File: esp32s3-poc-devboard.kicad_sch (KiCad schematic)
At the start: 23 parts, among them J1 24VDC, J2 Conn_01x01_Pin, U1 ESP32-S3, U2 AMS1117-3.3, U3 XC6206P332MR, U4 TPS5430DDA

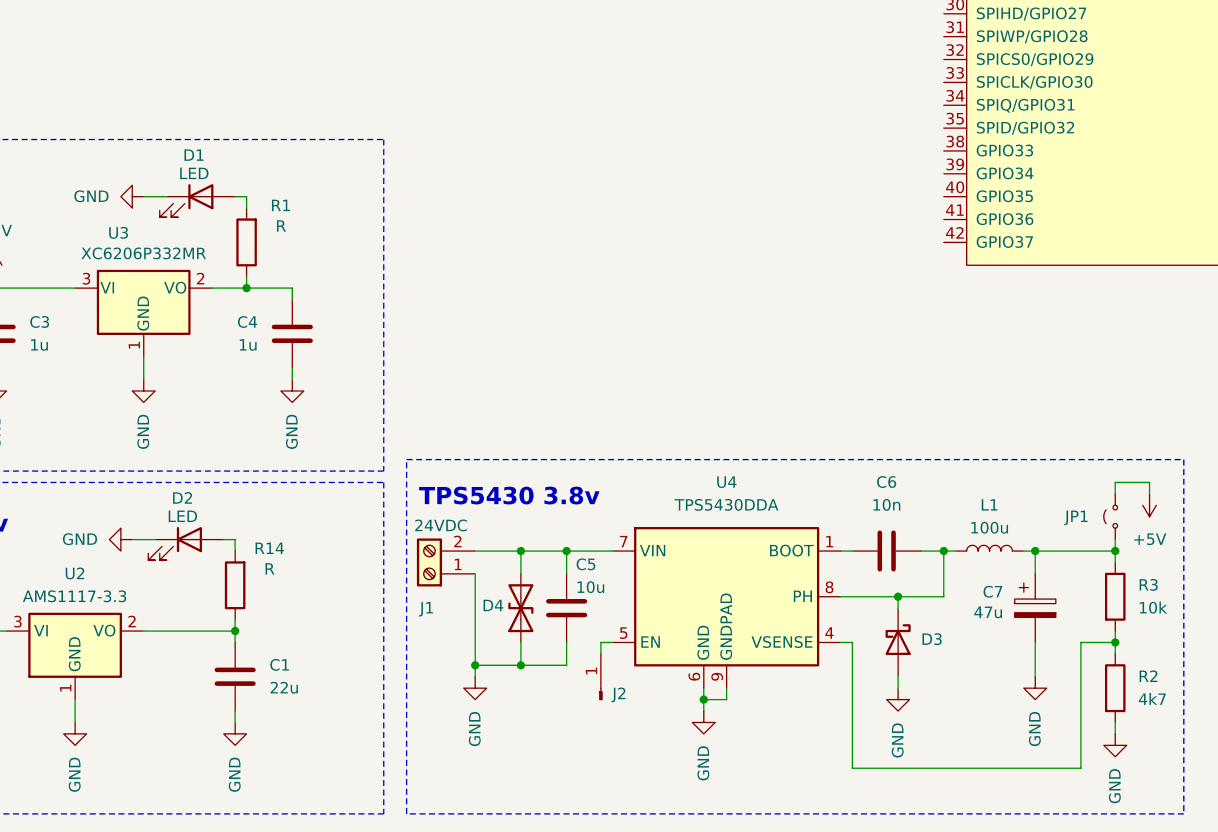
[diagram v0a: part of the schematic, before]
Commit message: add 3v3 power selection jumper
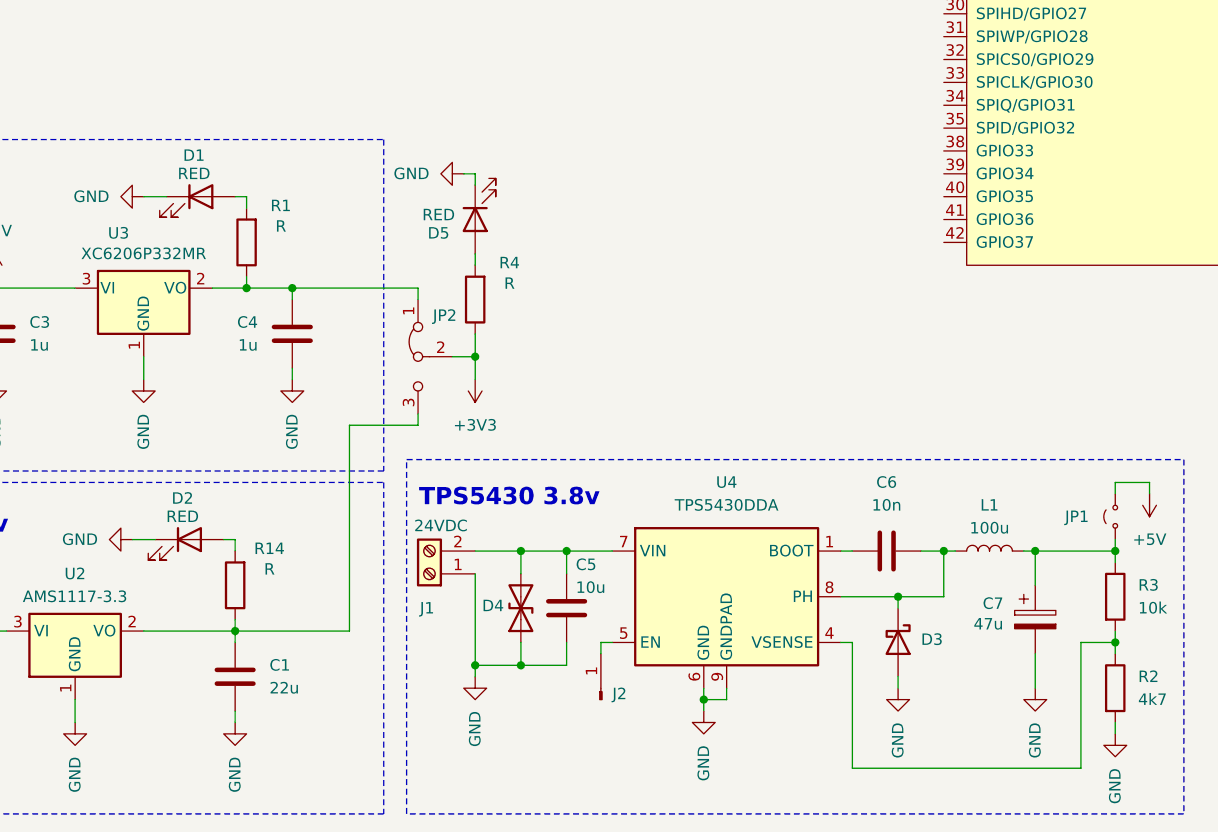
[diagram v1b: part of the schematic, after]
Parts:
- added D5: RED, symbol Device:LED
- added JP2: Jumper_3_Bridged12, symbol Jumper:Jumper_3_Bridged12
- added R4: R, symbol Device:R
- D1, D2: value LED -> RED
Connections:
- net GND: now also D5.1 (K)
- net at C4.1, R1.1, U3.2 (VO): now also JP2.1 (A)
- net at C1.1, R14.1, U2.2 (VO): now also JP2.3 (B)
- new net: D5.2 (A), R4.2
- new net +3V3: JP2.2 (C), R4.1
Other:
- moved on the sheet: C7

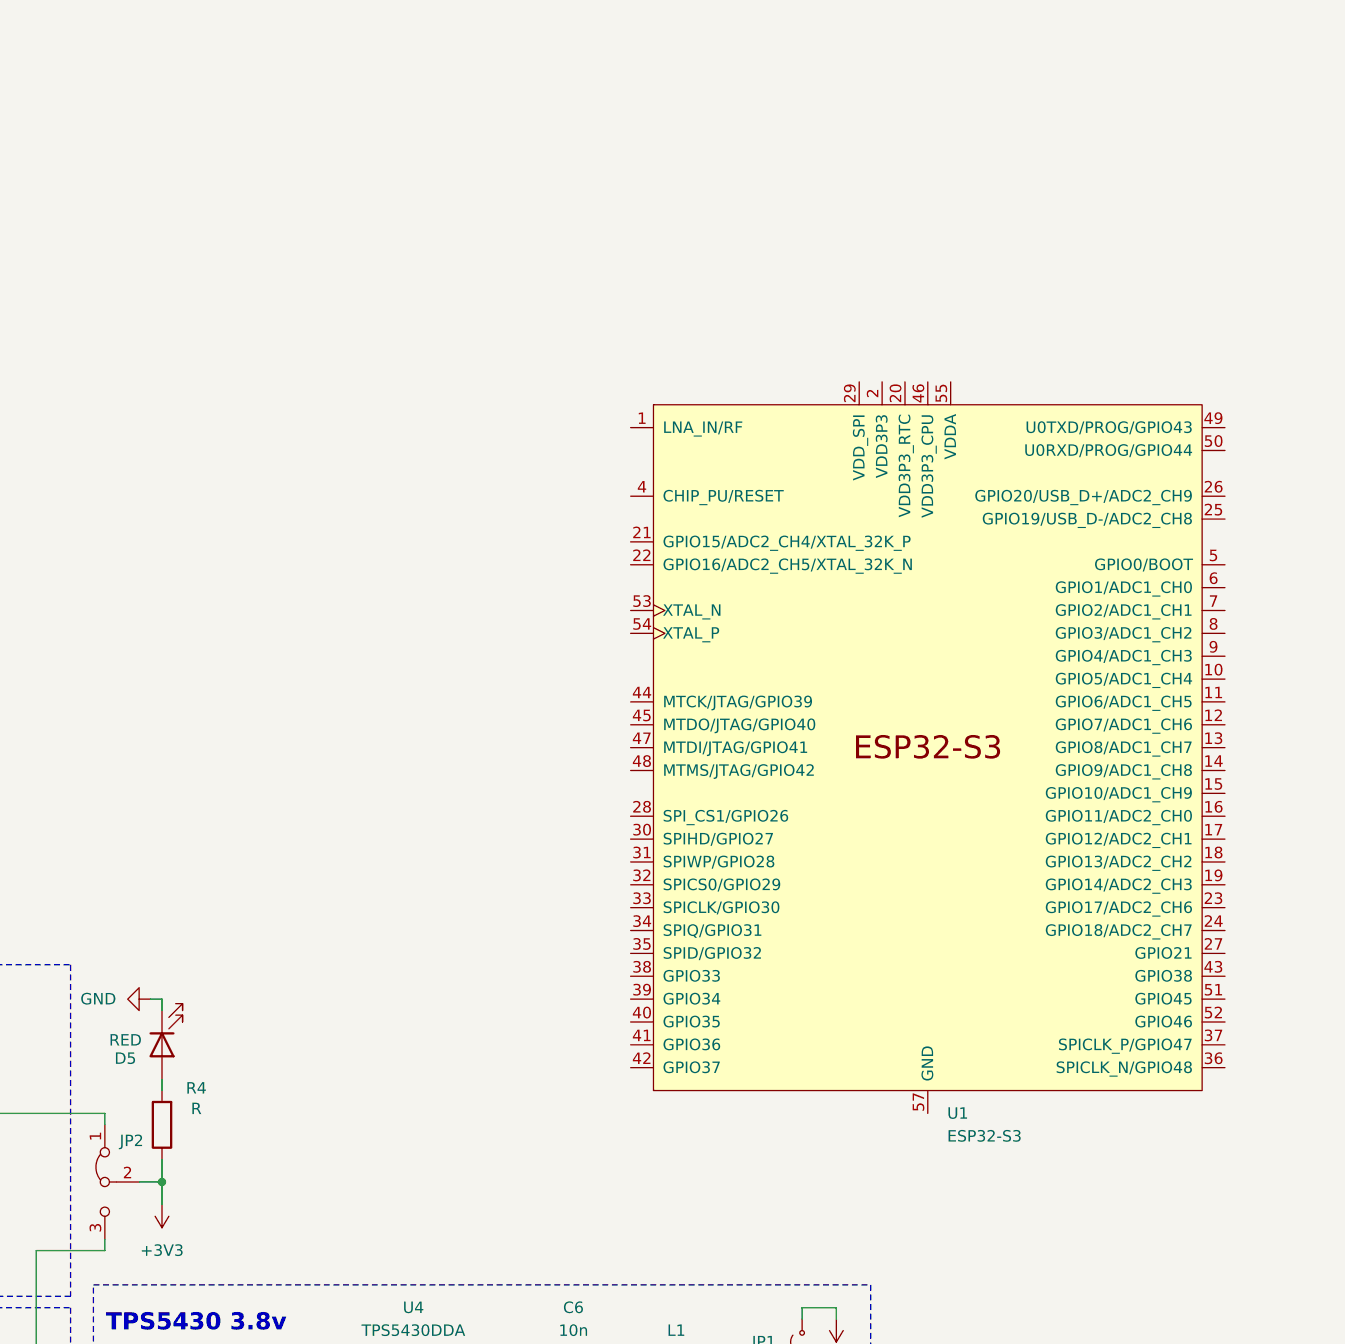
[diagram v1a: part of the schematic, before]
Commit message: add mcu power strapping capacitors
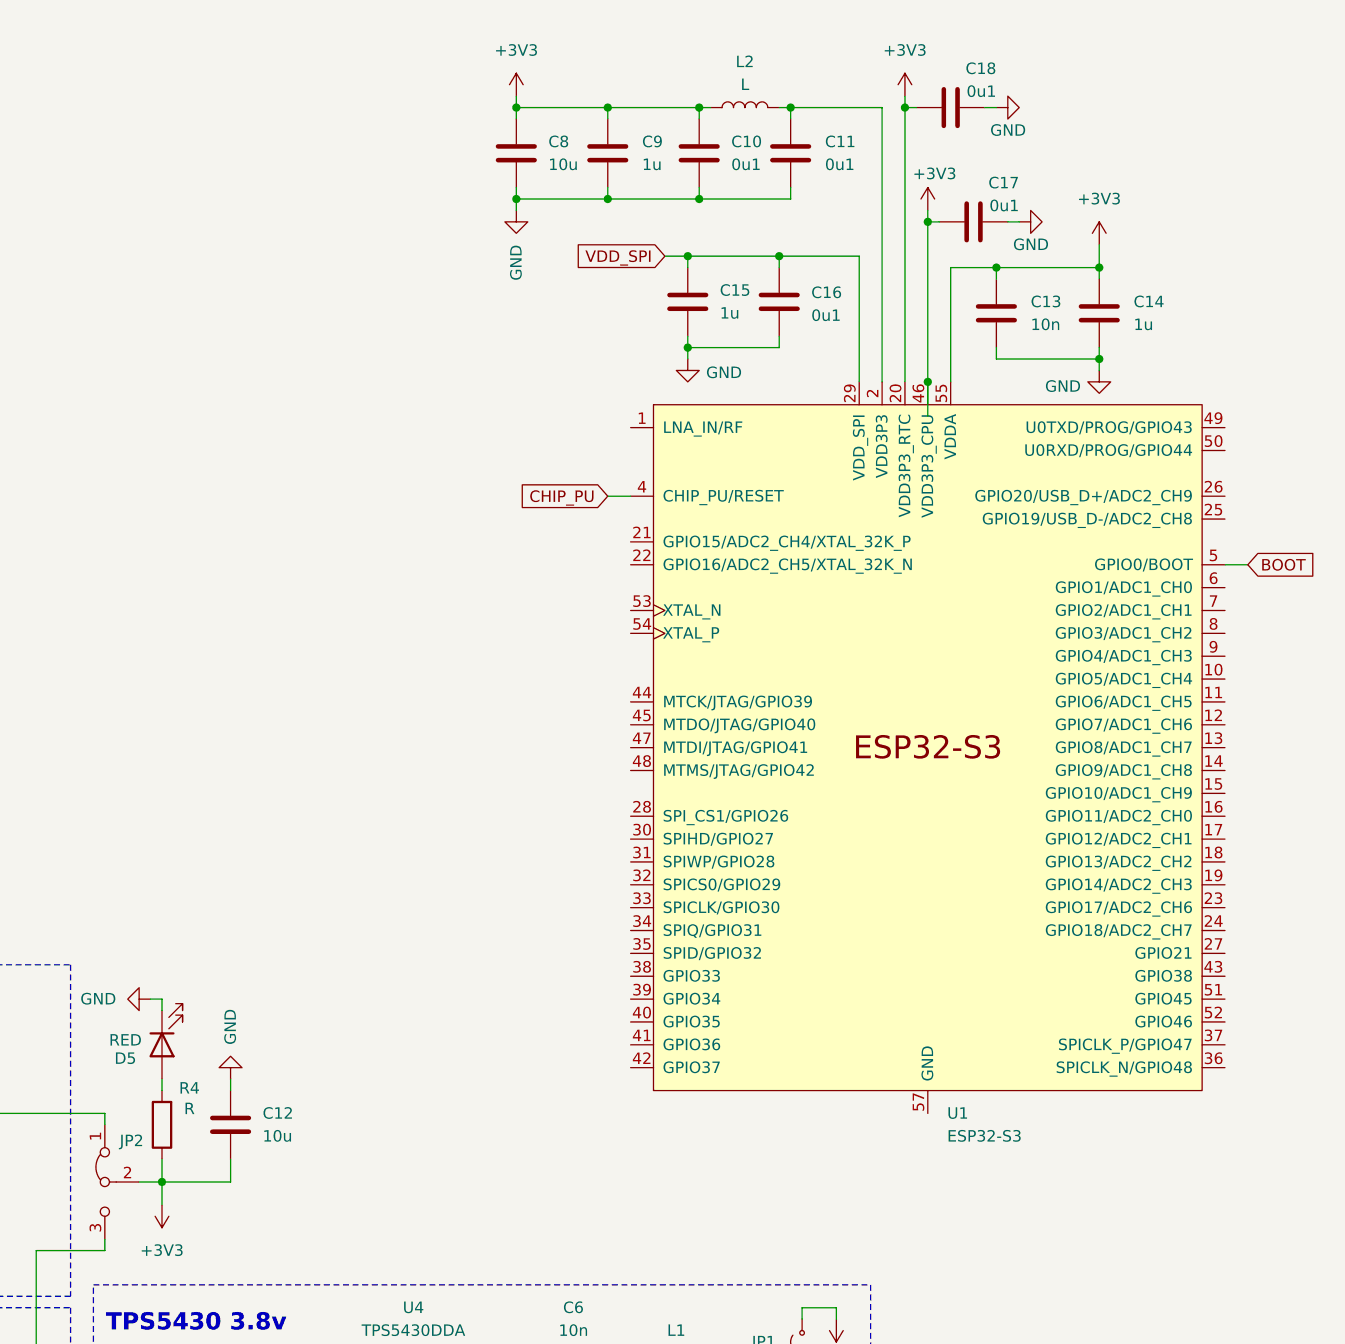
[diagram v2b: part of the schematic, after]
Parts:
- added C10, C11, C16, C17, C18: 0u1, symbol Device:C
- added C12, C8: 10u, symbol Device:C
- added C13: 10n, symbol Device:C
- added C14, C15, C9: 1u, symbol Device:C
- added L2: L, symbol Device:L
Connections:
- net +3V3: now also U1.20 (VDD3P3_RTC), U1.46 (VDD3P3_CPU), U1.55 (VDDA), U1.56 (VDDA), C10.1, C12.2, C13.1, C14.1, C17.1, C18.1, C8.1, C9.1, L2.1
- net GND: now also C10.2, C11.2, C12.1, C13.2, C14.2, C15.2, C16.2, C17.2, C18.2, C8.2, C9.2
- net VDD3P3: now also C11.1, L2.2
- net VDD_SPI: now reaches U1.29 (VDD_SPI)
- net VDD_SPI: now also C15.1, C16.1
- net CHIP_PU: now reaches U1.4 (CHIP_PU/RESET)
- net BOOT: now reaches U1.5 (GPIO0/BOOT)

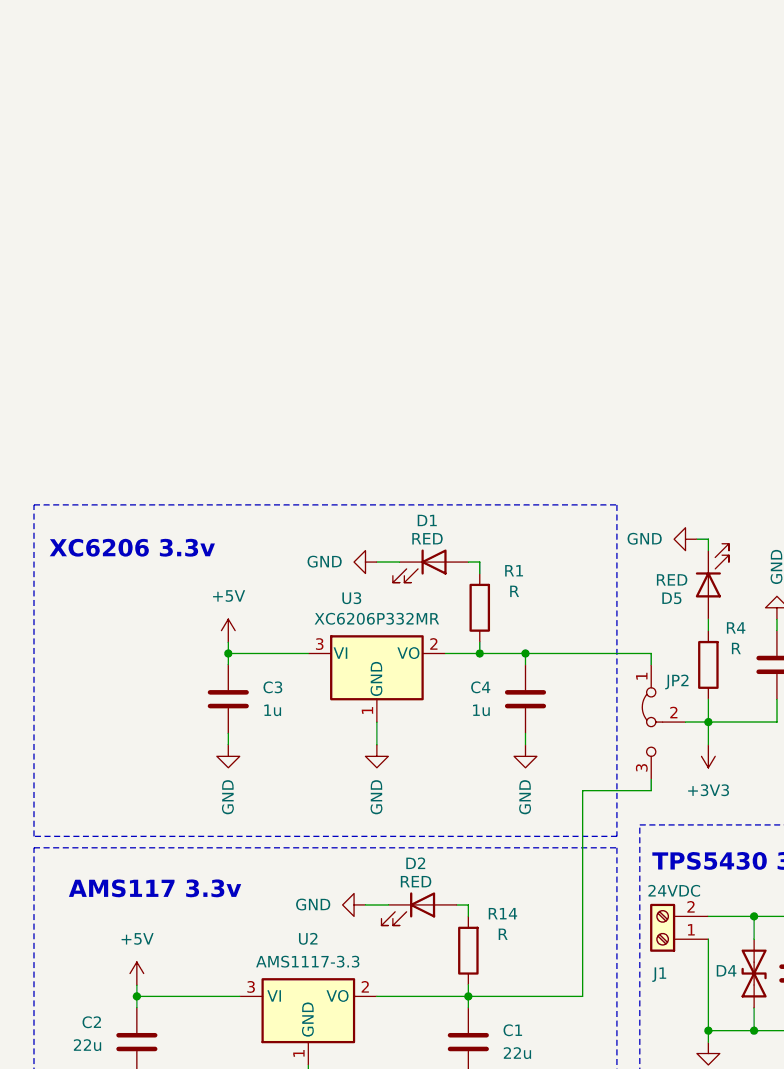
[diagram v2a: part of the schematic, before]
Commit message: add auto program circuit
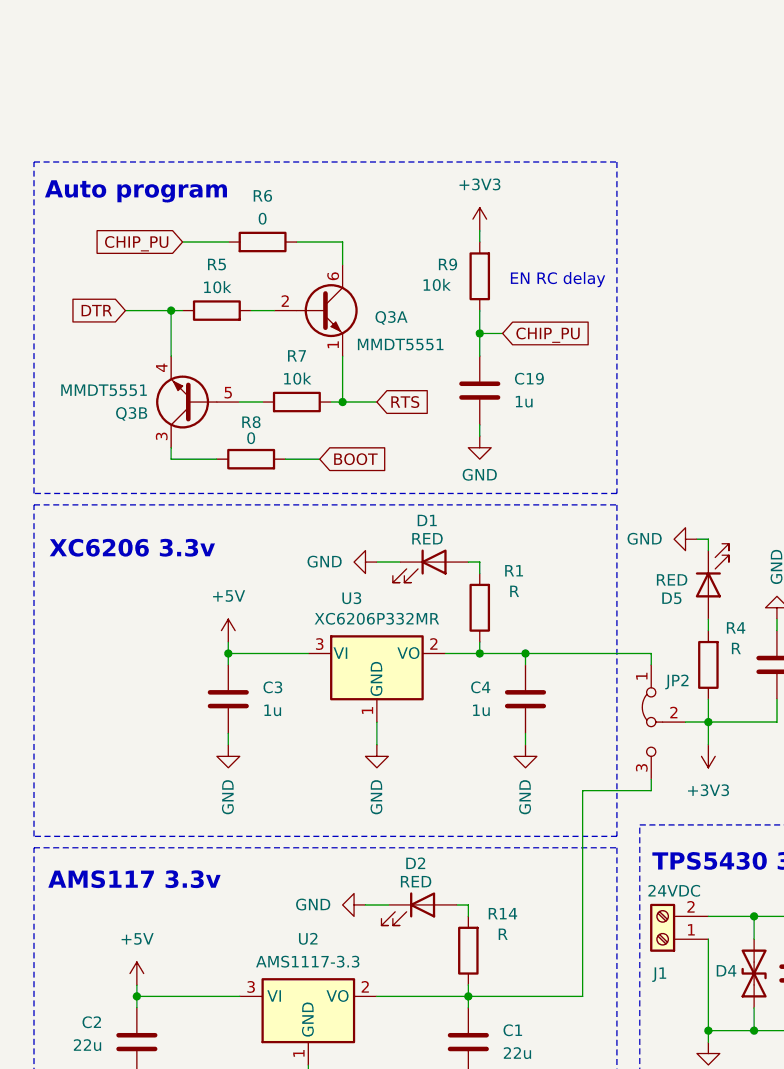
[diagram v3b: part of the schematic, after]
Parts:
- added C19: 1u, symbol Device:C
- added Q3: MMDT5551, Package_TO_SOT_SMD:SOT-363_SC-70-6, symbol Transistor_BJT:MMDT5551
- added R5, R7, R9: 10k, symbol Device:R
- added R6, R8: 0, symbol Device:R
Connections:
- net +3V3: now also R9.2
- net BOOT: now also R8.2
- net CHIP_PU: now also C19.1, R6.2, R9.1
- net GND: now also C19.2
- new net: Q3.6 (C1), R6.1
- new net: Q3.5 (B2), R7.2
- new net: Q3.3 (C2), R8.1
- new net: Q3.2 (B1), R5.2
- new net DTR: Q3.4 (E2), R5.1
- new net RTS: Q3.1 (E1), R7.1
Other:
- note added: "Auto program"
- note added: "EN RC delay"
